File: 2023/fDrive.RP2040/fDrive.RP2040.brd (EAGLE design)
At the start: 68 x 58 mm, 11 parts

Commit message: update
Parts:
- removed WRITE_DISABLED: (no value), microbuilder:SOLDERJUMPER_ARROW_NOPASTE
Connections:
- removed net MCU_VCC_5V: MCU_LEFT_SIDE.7
- removed net WP: FLASH_AT25SF321B_4MB.3, WRITE_DISABLED.2
- net GND: no longer WRITE_DISABLED.1
- net VCC_33: now also FLASH_AT25SF321B_4MB.3
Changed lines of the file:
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@@
 <grid distance="0.0025" unitdist="inch" unit="inch" style="dots" multiple="1" display="yes" altdistance="0.5" altunitdist="mm" altunit="mm"/>
 <layers>
-<layer number="1" name="Top" color="4" fill="1" visible="no" active="yes"/>
+<layer number="1" name="Top" color="4" fill="1" visible="yes" active="yes"/>
 <layer number="16" name="Bottom" color="1" fill="1" visible="yes" active="yes"/>
 <layer number="17" name="Pads" color="2" fill="1" visible="yes" active="yes"/>
@@
 <attribute name="VALUE" x="53.44855" y="25.08" size="1.27" layer="27" ratio="10" rot="R180"/>
 </element>
-<element name="WRITE_DISABLED" library="microbuilder" package="SOLDERJUMPER_ARROW_NOPASTE" value="" x="18" y="41" smashed="yes" rot="R90">
-<attribute name="BOM" value="EXCLUDE" x="18" y="41" size="1.778" layer="27" rot="R90" display="off"/>
-<attribute name="NAME" x="15.73" y="40.222" size="0.8128" layer="25" ratio="18" rot="R90" align="center"/>
-<attribute name="VALUE" x="19.651" y="39.349" size="0.4064" layer="27" ratio="10" rot="R90"/>
-</element>
 <element name="FLASH_AT25SF321B_4MB" library="microchip" library_urn="urn:adsk.eagle:library:294" package="SO-08" package3d_urn="urn:adsk.eagle:package:20804/2" value="25AA080SN" x="33" y="40" smashed="yes" rot="R270">
 <attribute name="MF" value="MICROCHIP" x="33" y="40" size="1.778" layer="27" rot="R270" display="off"/>
@@
 <contactref element="MCU_LEFT_SIDE" pad="6"/>
 <contactref element="FLASH_AT25SF321B_4MB" pad="4"/>
-<contactref element="WRITE_DISABLED" pad="1"/>
 <wire x1="30.4" y1="38.095" x2="63.08" y2="32" width="0" layer="19" extent="1-1"/>
-<wire x1="18" y1="39.984" x2="30.4" y2="38.095" width="0" layer="19" extent="1-1"/>
-<wire x1="5.8095" y1="49.71525" x2="18" y2="39.984" width="0" layer="19" extent="1-1"/>
+<wire x1="5.8095" y1="49.71525" x2="30.4" y2="38.095" width="0" layer="19" extent="1-1"/>
 </signal>
 <signal name="VCC_33">
@@
 <contactref element="FLASH_AT25SF321B_4MB" pad="8"/>
 <contactref element="FLASH_AT25SF321B_4MB" pad="7"/>
+<contactref element="FLASH_AT25SF321B_4MB" pad="3"/>
 <wire x1="60.54" y1="32" x2="61.0885" y2="65.291959375" width="0" layer="19" extent="1-1"/>
 <wire x1="35.6" y1="40.635" x2="60.54" y2="32" width="0" layer="19" extent="1-1"/>
 <wire x1="35.6" y1="41.905" x2="35.6" y2="40.635" width="0" layer="19" extent="1-1"/>
+<wire x1="30.4" y1="39.365" x2="35.6" y2="40.635" width="0" layer="19" extent="1-1"/>
 </signal>
 <signal name="MCU_D6">
@@
 <wire x1="35.6" y1="38.095" x2="58" y2="32" width="0" layer="19" extent="1-1"/>
 </signal>
-<signal name="MCU_VCC_5V">
-<contactref element="MCU_LEFT_SIDE" pad="7"/>
-</signal>
 <signal name="RA_1">
 <contactref element="R_ARRAY_8" pad="2"/>
@@
 <wire x1="18.7488" y1="22.2606" x2="5.8095" y2="34.47525" width="0" layer="19" extent="1-1"/>
 </signal>
-<signal name="WP">
-<contactref element="FLASH_AT25SF321B_4MB" pad="3"/>
-<contactref element="WRITE_DISABLED" pad="2"/>
-<wire x1="18" y1="42.016" x2="30.4" y2="39.365" width="0" layer="19" extent="1-1"/>
-</signal>
 <signal name="RA_7">

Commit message: 2023.2. PCBs
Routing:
- net VCC_33: track 0.00 -> 105.2 mm
- net GND: track 0.00 -> 72.5 mm
- net RA_1: track 0.00 -> 59.9 mm
- net MCU_D3: track 0.00 -> 54.4 mm
- net RA_5: track 0.00 -> 47.5 mm
- net MCU_D1: track 0.00 -> 37.0 mm, vias 0 -> 1
- net MCU_D4: track 0.00 -> 34.5 mm, vias 0 -> 1
- net MCU_D9_MISO: track 0.00 -> 34.0 mm, vias 0 -> 1
- net RA_7: track 0.00 -> 33.7 mm
- net RA_3: track 0.00 -> 33.2 mm
- net MCU_D2: track 0.00 -> 32.1 mm
- net MCU_D0: track 0.00 -> 31.2 mm
- net RA_2: track 0.00 -> 30.7 mm, vias 0 -> 1
- net MCU_D7_CS: track 0.00 -> 30.0 mm, vias 0 -> 1
- net MCU_D10_MOSI: track 0.00 -> 27.2 mm
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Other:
- board text added: "XIAO RP2040"

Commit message: Nusbio I2C Extension
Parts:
- removed FLASH_AT25SF321B_4MB: 25AA080SN, microchip:SO-08
- added FLASH_WINBOND_25Q128JV_16MB: (no value), microbuilder:SOIC8_208MIL
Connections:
- net GND: now also FLASH_WINBOND_25Q128JV_16MB.4; no longer FLASH_AT25SF321B_4MB.4
- net MCU_D10_MOSI: now also FLASH_WINBOND_25Q128JV_16MB.5; no longer FLASH_AT25SF321B_4MB.5
- net MCU_D7_CS: now also FLASH_WINBOND_25Q128JV_16MB.1; no longer FLASH_AT25SF321B_4MB.1
- net MCU_D8_SCK: now also FLASH_WINBOND_25Q128JV_16MB.6; no longer FLASH_AT25SF321B_4MB.6
- net MCU_D9_MISO: now also FLASH_WINBOND_25Q128JV_16MB.2; no longer FLASH_AT25SF321B_4MB.2
- net VCC_33: now also FLASH_WINBOND_25Q128JV_16MB.3, FLASH_WINBOND_25Q128JV_16MB.7, FLASH_WINBOND_25Q128JV_16MB.8; no longer FLASH_AT25SF321B_4MB.3, FLASH_AT25SF321B_4MB.7, FLASH_AT25SF321B_4MB.8
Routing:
- net VCC_33: track 105.2 -> 0.00 mm
- net GND: track 72.5 -> 0.00 mm
- net RA_1: track 59.9 -> 0.00 mm
- net MCU_D3: track 54.4 -> 0.00 mm
- net RA_5: track 47.5 -> 0.00 mm
- net MCU_D1: track 37.0 -> 0.00 mm, vias 1 -> 0
- net MCU_D4: track 34.5 -> 0.00 mm, vias 1 -> 0
- net MCU_D9_MISO: track 34.0 -> 0.00 mm, vias 1 -> 0
- net RA_7: track 33.7 -> 0.00 mm
- net RA_3: track 33.2 -> 0.00 mm
- net MCU_D2: track 32.1 -> 0.00 mm
- net MCU_D0: track 31.2 -> 0.00 mm
- net RA_2: track 30.7 -> 0.00 mm, vias 1 -> 0
- net MCU_D7_CS: track 30.0 -> 0.00 mm, vias 1 -> 0
- net MCU_D10_MOSI: track 27.2 -> 0.00 mm
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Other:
- board text added: "CS"
- board text added: "HOLD"
- board text added: "SCK"
- board text added: "WP"

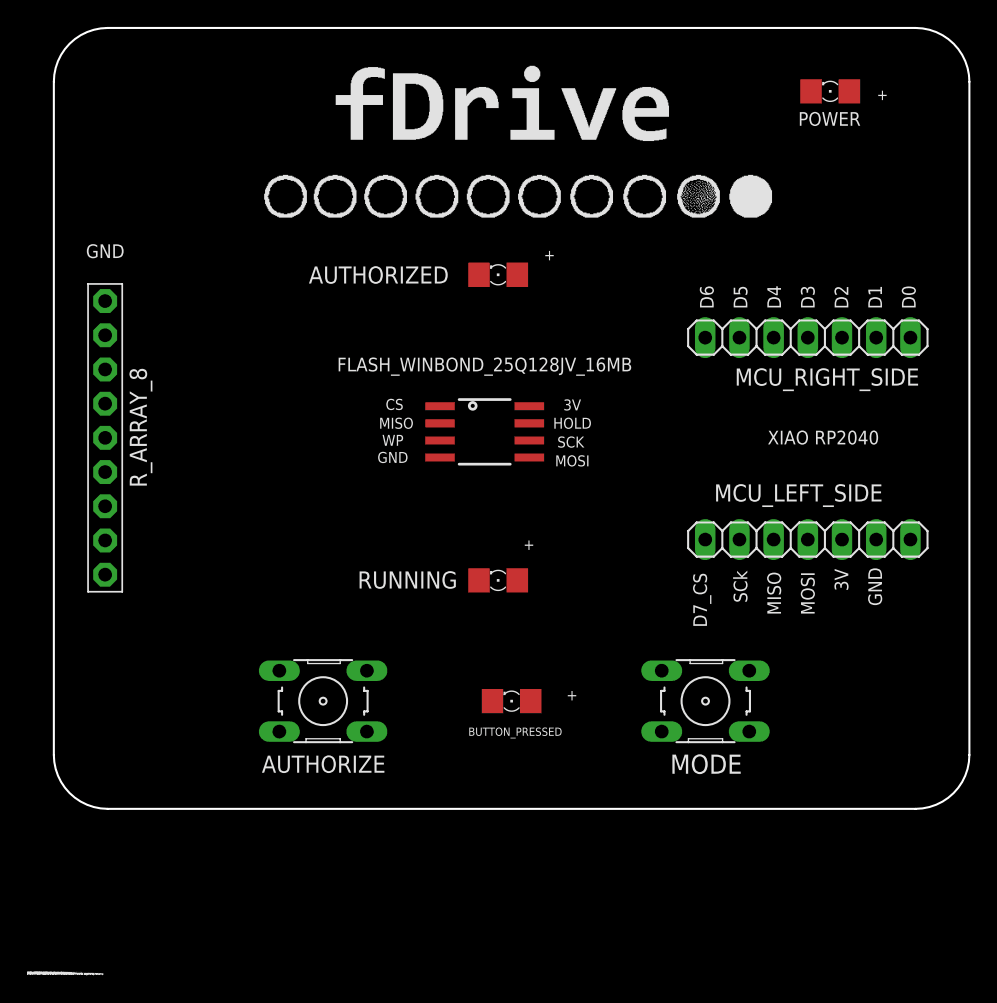
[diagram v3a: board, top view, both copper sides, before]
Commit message: Finishh and send board for summer 2023 to jlpcb
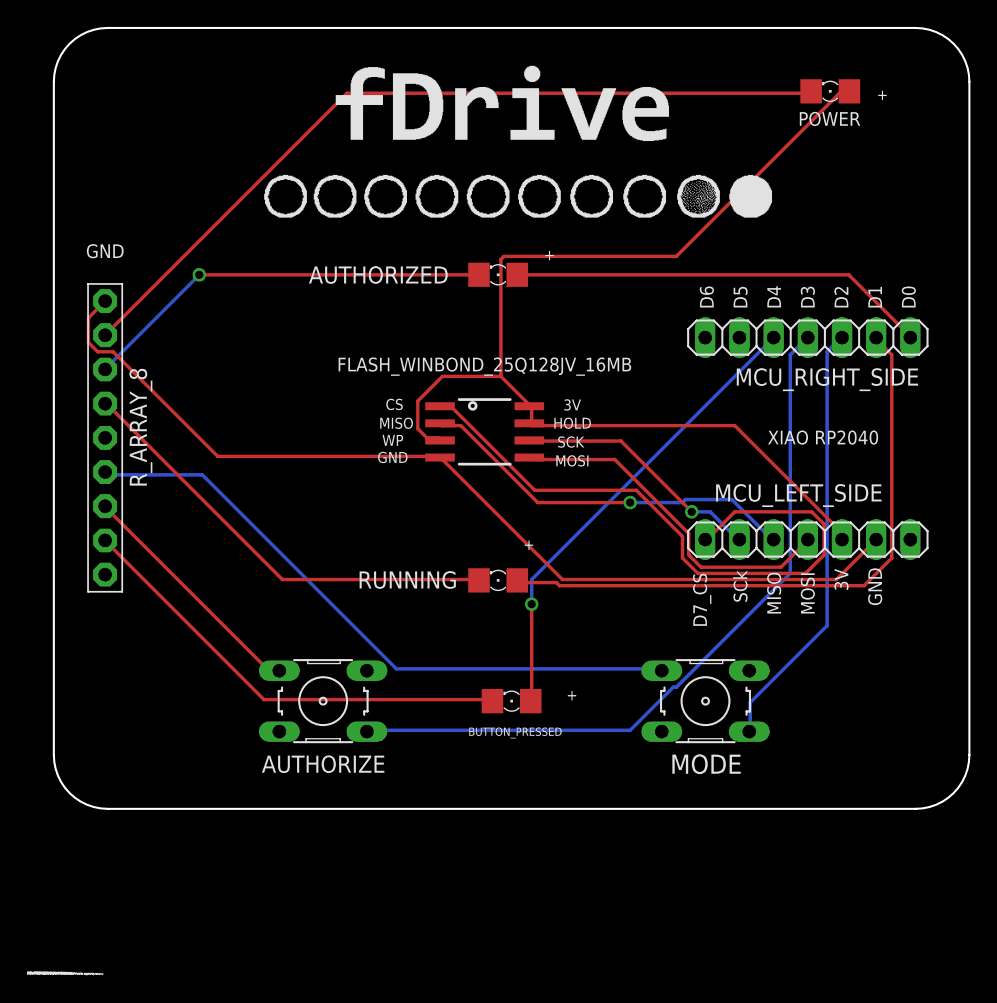
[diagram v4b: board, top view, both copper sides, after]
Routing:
- net VCC_33: track 0.00 -> 82.6 mm
- net GND: track 0.00 -> 70.6 mm
- net RA_1: track 0.00 -> 59.9 mm
- net MCU_D3: track 0.00 -> 54.4 mm
- net RA_5: track 0.00 -> 47.5 mm
- net MCU_D7_CS: track 0.00 -> 47.5 mm
- net MCU_D1: track 0.00 -> 45.7 mm
- net MCU_D4: track 0.00 -> 34.5 mm, vias 0 -> 1
- net RA_7: track 0.00 -> 33.7 mm
- net RA_3: track 0.00 -> 33.2 mm
- net MCU_D2: track 0.00 -> 32.1 mm
- net MCU_D0: track 0.00 -> 31.2 mm
- net RA_2: track 0.00 -> 30.7 mm, vias 0 -> 1
- net MCU_D9_MISO: track 0.00 -> 28.5 mm, vias 0 -> 1
- net MCU_D10_MOSI: track 0.00 -> 25.9 mm
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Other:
- board text added: "PCBv2 - 2023.6"
- board text removed: "PCBv1 - 2023.1"
